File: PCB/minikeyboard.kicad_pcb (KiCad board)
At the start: 2 copper layers, 59.5 x 60.8 mm, 11 parts, among them SW1 SW_Push, SW2 SW_Push, SW3 SW_Push, SW4 SW_Push, SW5 SW_Push, SW6 SW_Push, SW7 SW_Push, U1 XIAO-RP2040-DIP

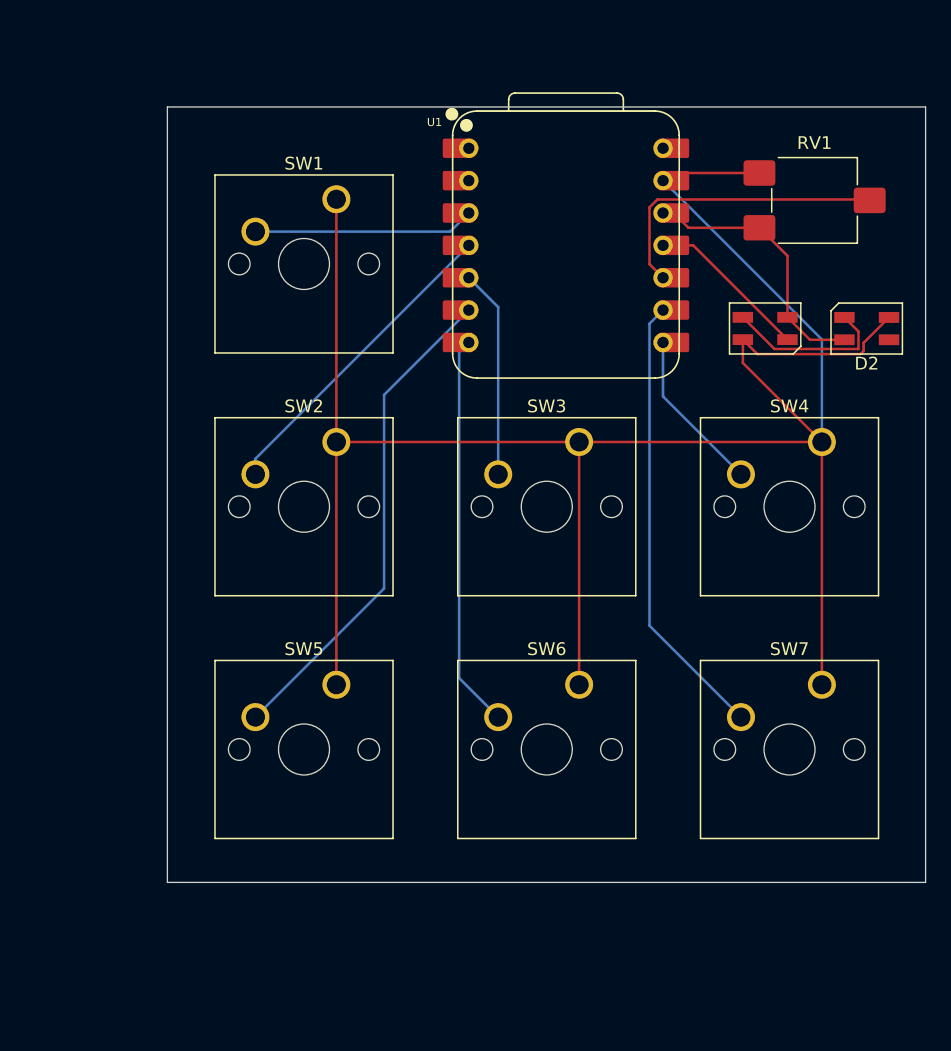
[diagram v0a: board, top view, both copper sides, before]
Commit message: Complete overhaul of the layout, parts and case
for better use and higher quality
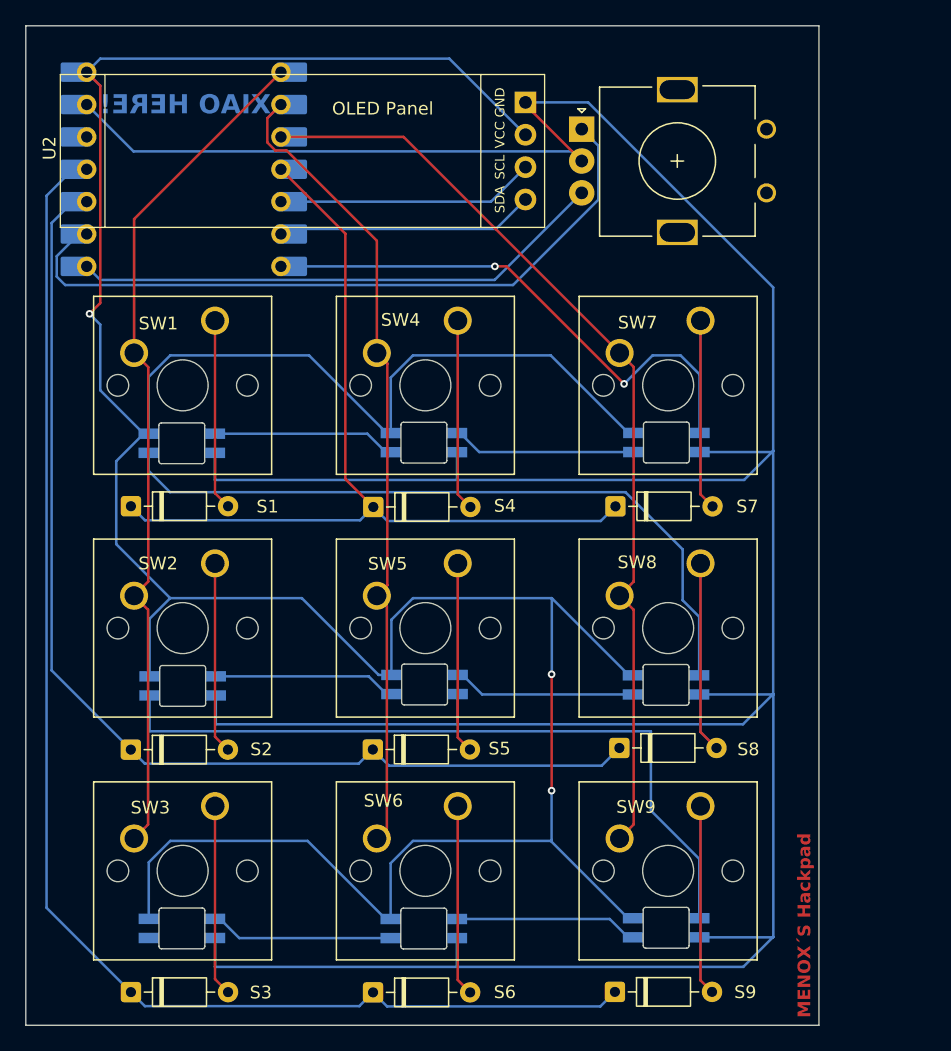
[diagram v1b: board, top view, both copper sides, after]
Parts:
- removed RV1: R_Potentiometer, Potentiometer_SMD:Potentiometer_ACP_CA6-VSMD_Vertical
- added D3: SK6812MINI, led:LED_SK6812MINI-E_PLCC4_3.2x2.8mm_P1.5mm, B.Cu at (69.0, 106.9)
- added D4: SK6812MINI, led:LED_SK6812MINI-E_PLCC4_3.2x2.8mm_P1.5mm, B.Cu at (88.0, 68.8)
- added D5: SK6812MINI, led:LED_SK6812MINI-E_PLCC4_3.2x2.8mm_P1.5mm, B.Cu at (88.0, 87.8)
- added D6: SK6812MINI, led:LED_SK6812MINI-E_PLCC4_3.2x2.8mm_P1.5mm, B.Cu at (88.0, 106.9)
- added D7: SK6812MINI, led:LED_SK6812MINI-E_PLCC4_3.2x2.8mm_P1.5mm, B.Cu at (107.0, 68.8)
- added D8: SK6812MINI, led:LED_SK6812MINI-E_PLCC4_3.2x2.8mm_P1.5mm, B.Cu at (107.0, 87.8)
- added D9: SK6812MINI, led:LED_SK6812MINI-E_PLCC4_3.2x2.8mm_P1.5mm, B.Cu at (107.0, 106.9)
- added G***: LOGO, led:patrick, B.Cu at (91.7, 45.9)
- added G***: LOGO, led:spongebob, B.Cu at (83.8, 47.1)
- added G***: LOGO, led:jerry, B.Cu at (107.6, 46.6)
- added S1: 1N4148, Diode_THT:D_DO-35_SOD27_P7.62mm_Horizontal, F.Cu at (65.0, 73.8)
- added S2: 1N4148, Diode_THT:D_DO-35_SOD27_P7.62mm_Horizontal, F.Cu at (65.0, 92.9)
- added S3: 1N4148, Diode_THT:D_DO-35_SOD27_P7.62mm_Horizontal, F.Cu at (65.0, 111.9)
- added S4: 1N4148, Diode_THT:D_DO-35_SOD27_P7.62mm_Horizontal, F.Cu at (84.0, 73.8)
- added S5: 1N4148, Diode_THT:D_DO-35_SOD27_P7.62mm_Horizontal, F.Cu at (84.0, 92.9)
- added S6: 1N4148, Diode_THT:D_DO-35_SOD27_P7.62mm_Horizontal, F.Cu at (84.0, 111.9)
- added S7: 1N4148, Diode_THT:D_DO-35_SOD27_P7.62mm_Horizontal, F.Cu at (103.0, 73.8)
- added S8: 1N4148, Diode_THT:D_DO-35_SOD27_P7.62mm_Horizontal, F.Cu at (103.3, 92.8)
- added S9: 1N4148, Diode_THT:D_DO-35_SOD27_P7.62mm_Horizontal, F.Cu at (103.0, 111.9)
- added SW10: RotaryEncoder, Rotary_Encoder:RotaryEncoder_Alps_EC11E_Vertical_H20mm, F.Cu at (100.4, 44.2)
- added SW8: SW_Push, Button_Switch_Keyboard:SW_Cherry_MX_1.00u_PCB, F.Cu at (109.7, 78.3)
- added SW9: SW_Push, Button_Switch_Keyboard:SW_Cherry_MX_1.00u_PCB, F.Cu at (109.7, 97.3)
- added U2: OLED_0.96_I2C, oled:SSD1306-0.91-OLED-4pin-128x32, F.Cu at (59.5, 39.9)
- D1, D2: footprint LED_SMD:LED_SK6812MINI_PLCC4_3.5x3.5mm_P1.75mm -> led:LED_SK6812MINI-E_PLCC4_3.2x2.8mm_P1.5mm; moved to B.Cu
- U1: moved to B.Cu
- moved D2 60.6 mm to (69.1, 87.9)
- moved D1 46.7 mm to (69.0, 68.8), turned to 180 degrees
- moved SW3 40.4 mm to (71.6, 97.3)
- moved U1 30.6 mm to (69.2, 47.3), turned to 180 degrees
- moved SW4 30.1 mm to (90.6, 59.2)
- moved SW7 30.1 mm to (109.7, 59.2)
- moved SW2 13.5 mm to (71.6, 78.3)
- moved SW6 13.5 mm to (90.6, 97.3)
- moved SW5 13.5 mm to (90.6, 78.3)
- moved SW1 13.5 mm to (71.6, 59.2)
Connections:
- D1 pad 1: Net-(D1-DOUT) -> GND
- D1 pad 2: GND -> Net-(D1-DIN)
- D1 pad 3: Net-(D1-DIN) -> VBUS
- D1 pad 4: +3.3V -> Net-(D1-DOUT)
- D2 pad 1: unconnected-(D2-DOUT-Pad1) -> GND
- D2 pad 2: GND -> Net-(D2-DIN)
- D2 pad 3: Net-(D1-DOUT) -> VBUS
- D2 pad 4: +3.3V -> Net-(D2-DOUT)
- SW1 pad 1: GND -> Net-(S1-A)
- SW1 pad 2: Net-(U1-GPIO28/ADC2/A2) -> COL1
- SW2 pad 1: GND -> Net-(S2-A)
- SW2 pad 2: Net-(U1-GPIO29/ADC3/A3) -> COL1
- SW3 pad 1: GND -> Net-(S3-A)
- SW3 pad 2: Net-(U1-GPIO6/SDA) -> COL1
- SW4 pad 1: GND -> Net-(S4-A)
- SW4 pad 2: Net-(U1-GPIO1/RX) -> COL2
- SW5 pad 1: GND -> Net-(S5-A)
- SW5 pad 2: Net-(U1-GPIO7/SCL) -> COL2
- SW6 pad 1: GND -> Net-(S6-A)
- SW6 pad 2: Net-(U1-GPIO0/TX) -> COL2
- SW7 pad 1: GND -> Net-(S7-A)
- SW7 pad 2: Net-(U1-GPIO2/SCK) -> COL3
- U1 pad 1: Net-(D3-DIN) -> COL1
- U1 pad 10: Net-(U1-GPIO4/MISO) -> ROW2
- U1 pad 11: Net-(D1-DIN) -> ROW3
- U1 pad 12: +3.3V -> +3V3
- U1 pad 14: unconnected-(U1-VBUS-Pad14) -> VBUS
- U1 pad 2: unconnected-(U1-GPIO27/ADC1/A1-Pad2) -> COL2
- U1 pad 3: Net-(U1-GPIO28/ADC2/A2) -> COL3
- U1 pad 4: Net-(U1-GPIO29/ADC3/A3) -> ROW1
- U1 pad 5: Net-(U1-GPIO6/SDA) -> SDA
- U1 pad 6: Net-(U1-GPIO7/SCL) -> SCL
- U1 pad 7: Net-(U1-GPIO0/TX) -> LEDS
- U1 pad 8: Net-(U1-GPIO1/RX) -> RotEncB
- U1 pad 9: Net-(U1-GPIO2/SCK) -> RotEncA
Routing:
- net VBUS: track 0.00 -> 263.4 mm, vias 0 -> 3
- net GND: track 171.1 -> 288.9 mm
- net ROW3: track 0.00 -> 109.1 mm
- net ROW2: track 0.00 -> 87.7 mm
- net COL3: track 0.00 -> 73.5 mm
- net ROW1: track 0.00 -> 69.3 mm
- net COL1: track 0.00 -> 66.7 mm
- net COL2: track 0.00 -> 63.4 mm
- net Net-(D2-DOUT): track 0.00 -> 58.4 mm
- net RotEncA: track 0.00 -> 56.3 mm
- net Net-(D1-DOUT): track 13.0 -> 56.3 mm
- net LEDS: track 0.00 -> 42.8 mm, vias 0 -> 2
- net RotEncB: track 0.00 -> 42.1 mm
- net Net-(U1-GPIO7/SCL): track 38.9 -> 0.00 mm
- net Net-(U1-GPIO2/SCK): track 35.4 -> 0.00 mm
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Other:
- board size 59.5 x 60.8 mm -> 62.2 x 78.4 mm
- board text added: "MENOX´S Hackpad"
- board text added: "SW_Push"
- board text added: "XIAO HERE!"
- board text removed: "Keyboard by Menox Integrated Wlan and Bluetooth"
